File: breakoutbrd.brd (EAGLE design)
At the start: 69.3 x 99.7 mm, 6 parts

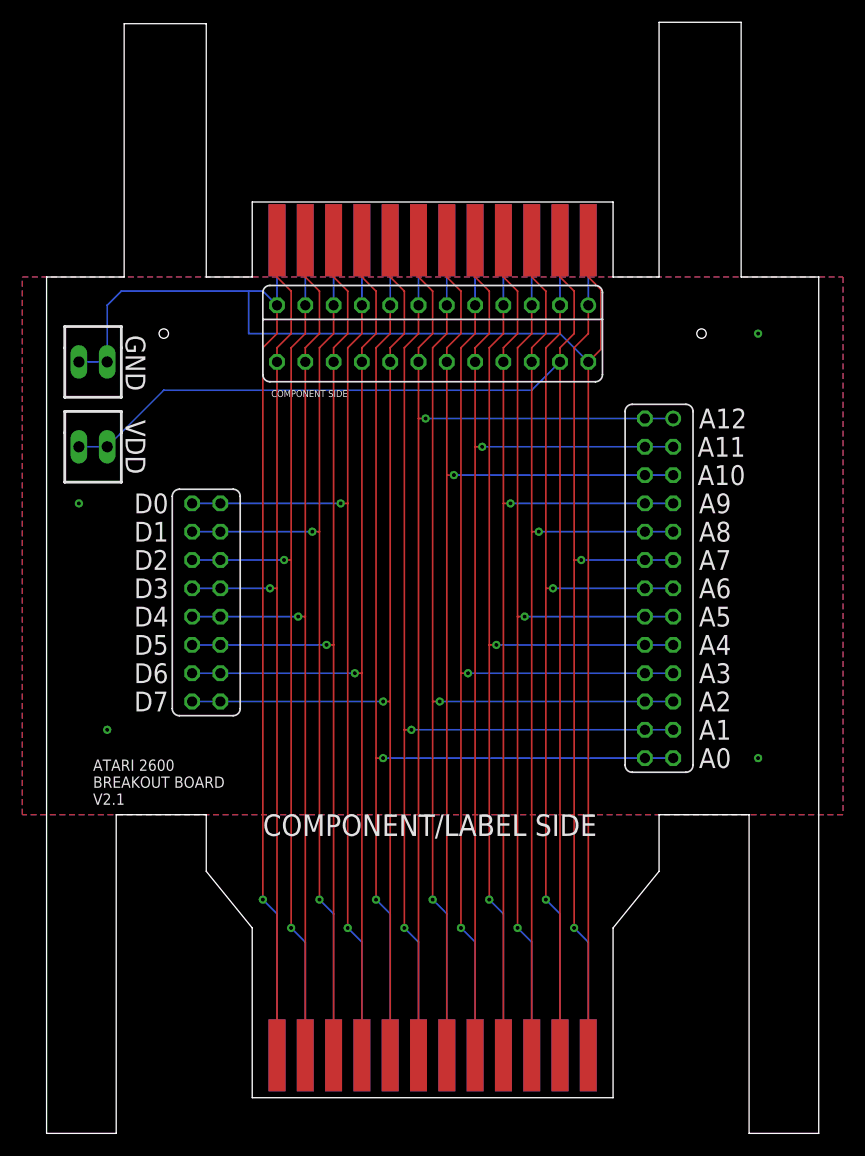
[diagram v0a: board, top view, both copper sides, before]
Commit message: Rework board to drive an STM32F4XX DevEBox from the cartridge edge
Keep only the lower edge fingers and their stubs; remove SV1, SV2, the
VDD/GND Molex headers, the U$1 socket, the top fingers, mounting holes,
ground pour and old labels. Flatten the top edge (tabs removed) at
y=83.82mm.

Add footprint U1 (STM32F4XX_DEVEBOX): the DevEBox rotated 90 deg CCW,
with 1.0mm through-holes at the matched header pins and its four 3.2mm
mounting holes. Route D0-D7 -> PD8-PD15, A0-A12 -> PE0-PE12, VDD -> 5V
and GND -> GND, and join the two GND fingers.

Schematic and library updated to match (parts removed, J1 limited to
pads 1-24, STM part added). Preview in breakout_stm_overlay.png.

Co-Authored-By: Claude Opus 5.5 <noreply@anthropic.com>
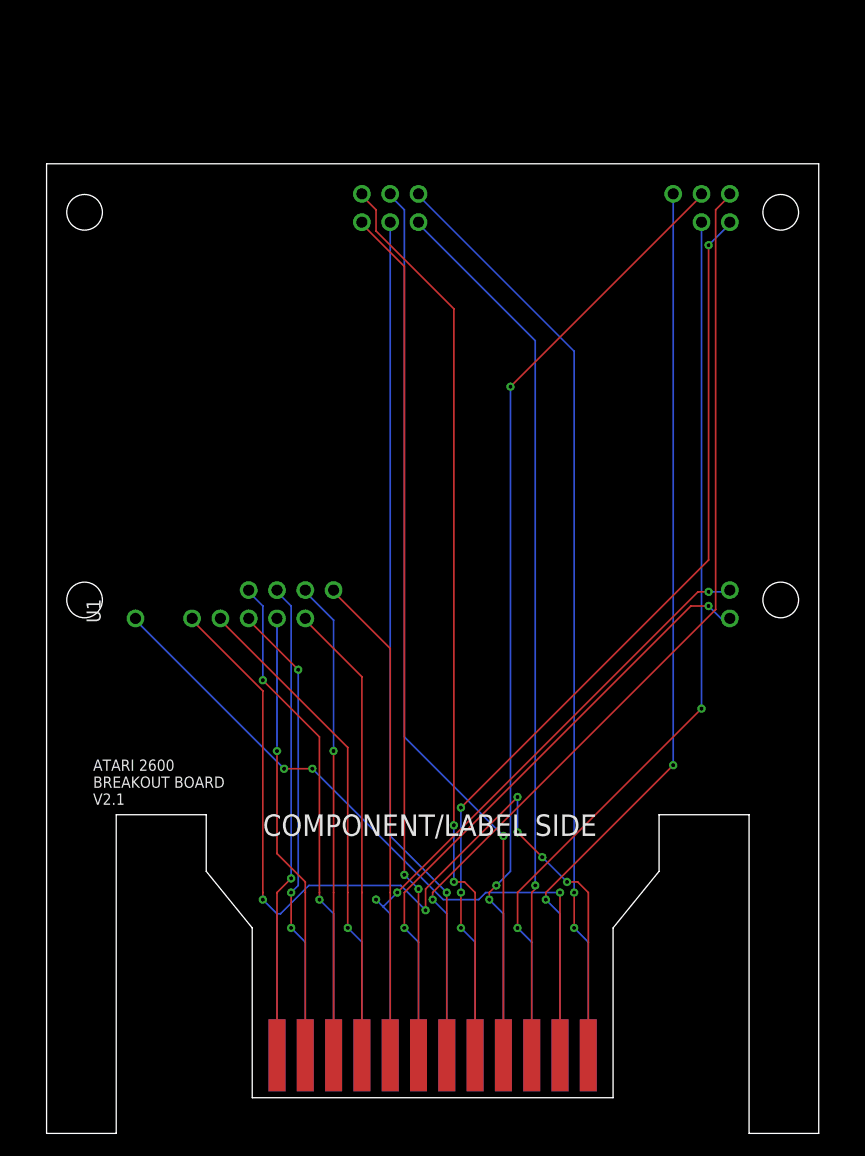
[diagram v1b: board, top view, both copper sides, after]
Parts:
- removed GND1, VDD: 22-23-2021, a26board:22-23-2021
- removed SV1: (no value), a26board:FE08-2
- removed SV2: (no value), a26board:FE13-2
- removed U$1: EBC12DCWN, a26board:EBC12DCWN
- added U1: STM32F4XX, a26board:STM32F4XX_DEVEBOX
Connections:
- net CADDR0: now also U1.PE0; no longer J1.32, SV2.25, SV2.26, U$1.8
- net CADDR1: now also U1.PE1; no longer J1.31, SV2.23, SV2.24, U$1.7
- net CADDR10: now also U1.PE10; no longer J1.43, SV2.5, SV2.6, U$1.19
- net CADDR11: now also U1.PE11; no longer J1.44, SV2.3, SV2.4, U$1.20
- net CADDR12: now also U1.PE12; no longer J1.42, SV2.1, SV2.2, U$1.18
- net CADDR2: now also U1.PE2; no longer J1.30, SV2.21, SV2.22, U$1.6
- net CADDR3: now also U1.PE3; no longer J1.29, SV2.19, SV2.20, U$1.5
- net CADDR4: now also U1.PE4; no longer J1.28, SV2.17, SV2.18, U$1.4
- net CADDR5: now also U1.PE5; no longer J1.27, SV2.15, SV2.16, U$1.3
- net CADDR6: now also U1.PE6; no longer J1.26, SV2.13, SV2.14, U$1.2
- net CADDR7: now also U1.PE7; no longer J1.25, SV2.11, SV2.12, U$1.1
- net CADDR8: now also U1.PE8; no longer J1.46, SV2.10, SV2.9, U$1.22
- net CADDR9: now also U1.PE9; no longer J1.45, SV2.7, SV2.8, U$1.21
- net CDATA0: now also U1.PD8; no longer J1.33, SV1.15, SV1.16, U$1.9
- net CDATA1: now also U1.PD9; no longer J1.34, SV1.13, SV1.14, U$1.10
- net CDATA2: now also U1.PD10; no longer J1.35, SV1.11, SV1.12, U$1.11
- net CDATA3: now also U1.PD11; no longer J1.37, SV1.10, SV1.9, U$1.13
- net CDATA4: now also U1.PD12; no longer J1.38, SV1.7, SV1.8, U$1.14
- net CDATA5: now also U1.PD13; no longer J1.39, SV1.5, SV1.6, U$1.15
- net CDATA6: now also U1.PD14; no longer J1.40, SV1.3, SV1.4, U$1.16
- net CDATA7: now also U1.PD15; no longer J1.41, SV1.1, SV1.2, U$1.17
- net GND: now also U1.GND; no longer GND1.1, GND1.2, J1.36, J1.48, U$1.12, U$1.24
- net VDD: now also U1.5V; no longer J1.47, U$1.23, VDD.1, VDD.2
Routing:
- net GND: track 207.5 -> 97.5 mm, vias 5 -> 6
- net VDD: track 120.5 -> 63.4 mm, vias 0 -> 3
- net CDATA7: track 92.0 -> 43.7 mm, vias 1 -> 0
- net CDATA6: track 89.4 -> 41.2 mm, vias 1 -> 0
- net CDATA5: track 86.9 -> 42.6 mm
- net CDATA4: track 84.4 -> 40.1 mm
- net CDATA0: track 88.2 -> 44.3 mm, vias 2 -> 1
- net CADDR0: track 100.9 -> 57.3 mm, vias 2 -> 3
- net CADDR1: track 98.3 -> 55.5 mm
- net CDATA2: track 83.1 -> 41.7 mm, vias 2 -> 3
- net CDATA1: track 85.6 -> 44.7 mm
- net CDATA3: track 81.8 -> 42.6 mm
- net CADDR12: track 97.1 -> 76.7 mm, vias 1 -> 2
- net CADDR10: track 94.5 -> 76.7 mm
- net CADDR11: track 92.0 -> 81.9 mm, vias 1 -> 2
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- removed copper zone on layer 1, net GND
- removed copper zone on layer 16, net GND
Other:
- board size 69.3 x 99.7 mm -> 69.3 x 87 mm
- board text added: "STM32 overlay: rotated 90 CCW, pin 1 (5V) at left"
- board text removed: "A0"
- board text removed: "A1"
- board text removed: "A10"
- board text removed: "A11"
- board text removed: "A12"
- board text removed: "A2"
- board text removed: "A3"
- board text removed: "A4"
- board text removed: "A5"
- board text removed: "A6"
- board text removed: "A7"
- board text removed: "A8"
- board text removed: "A9"
- board text removed: "D0"
- board text removed: "D1"
- board text removed: "D2"
- board text removed: "D3"
- board text removed: "D4"
- board text removed: "D5"
- board text removed: "D6"
- board text removed: "D7"
- board text removed: "GND"
- board text removed: "VDD"
